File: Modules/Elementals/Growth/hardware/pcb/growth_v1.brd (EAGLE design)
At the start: 17.8 x 100 mm, 18 parts, among them J1 EURO_POWER, J2 WQP-PJ398SM6, J3 WQP-PJ398SM6, J4 WQP-PJ398SM6, J5 WQP-PJ398SM6, U1 TL072P

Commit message: Finalized(?)
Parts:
- R2, R3, R4, R6, R7, R8: device SonicAthame:0207/10 -> SonicAthame:0207/2V
- moved R7 21.6 mm to (1.91, 39.4), turned to 90 degrees
- moved R8 21.6 mm to (15.9, 39.4), turned to 270 degrees
- moved R3 14.0 mm to (1.91, 49.5)
- moved R4 7.01 mm to (8.89, 62.9), turned to 0 degrees
- moved R6 7.01 mm to (8.26, 24.1)
- moved C3 5.08 mm to (15.9, 44.5)
- moved C4 0.63 mm to (1.91, 45.1)
- moved R2 0.63 mm to (15.9, 49.5), turned to 270 degrees
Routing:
- net N$10: track 27.8 -> 6.77 mm
- net N$4: track 13.4 -> 31.5 mm
- net N$5: track 13.4 -> 3.65 mm
- net N$11: track 13.4 -> 3.65 mm
- net N$3: track 15.8 -> 6.77 mm
- net N$6: track 13.4 -> 21.8 mm
- net +12V: track 69.1 -> 73.7 mm
- net N$9: track 42.2 -> 39.0 mm
- net N$8: track 43.8 -> 46.1 mm
- net N$1: track 13.1 -> 10.9 mm
- net -12V: track 61.5 -> 62.8 mm
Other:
- board text added: "100x In"
- board text added: "100x Out"
- board text added: "100x Setting"
- board text added: "10x In"
- board text added: "10x Out"
- board text added: "10x Setting"
- board text added: "Elemental Growth"
- board text added: "Prototype v1"
- board text added: "Sonic Athame is fully open-hardware and open-software!! Find schematics and code on the official GitHub: https://github.com/nimaid/Sonic-Athame-eurorack"
- board text added: "Sonic Athame™"
- board text added: "The Point of Modular"

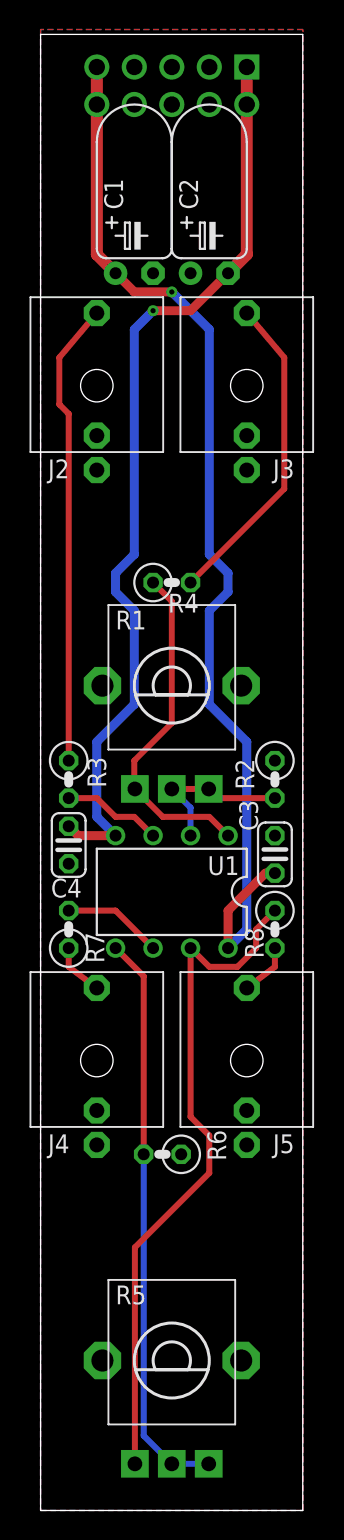
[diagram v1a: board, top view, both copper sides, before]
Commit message: Better power layout
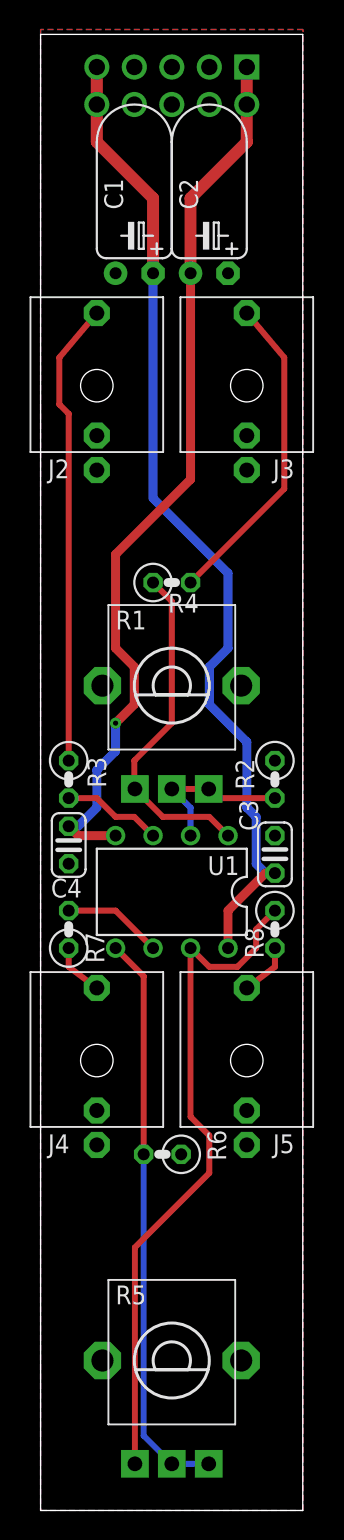
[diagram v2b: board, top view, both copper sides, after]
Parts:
- C1, C2: device SonicAthame:TT2D5L -> SonicAthame:TT2D5L_FLIP
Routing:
- net +12V: track 73.7 -> 67.8 mm, vias 1 -> 0
- net -12V: track 62.8 -> 61.3 mm
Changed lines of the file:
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@@
 </layers>
 <board>
-<fusionsync huburn="a.cGVyc29uYWw6dWUyZGY0M2Ex" projecturn="a.cGVyc29uYWw6dWUyZGY0M2ExIzIwMTkwODAzMjA2ODUyMzMx" f3durn="urn:adsk.wipprod:dm.lineage:vAaPX6FpQhacq-Y-F4SVOQ" pcbguid="a51a945c-d459-4631-a547-21d73037d6c1" lastpulledtime="" lastsyncedchangeguid="6d598e2e-e7a5-5e8d-0865-508f45d3280c"/>
+<fusionsync huburn="a.cGVyc29uYWw6dWUyZGY0M2Ex" projecturn="a.cGVyc29uYWw6dWUyZGY0M2ExIzIwMTkwODAzMjA2ODUyMzMx" f3durn="urn:adsk.wipprod:dm.lineage:vAaPX6FpQhacq-Y-F4SVOQ" pcbguid="a51a945c-d459-4631-a547-21d73037d6c1" lastpulledtime="" lastsyncedchangeguid="4652df98-1920-a6b8-155c-d7d488b7e636"/>
 <plain>
 <wire x1="0" y1="0" x2="17.76" y2="0" width="0" layer="20"/>
@@
 <attribute name="SPICEPREFIX" value="C" x="1.905" y="45.085" size="1.778" layer="27" rot="R270" display="off"/>
 </element>
-<element name="C1" library="SonicAthame" library_urn="urn:adsk.eagle:library:22327399" package="TT2D5L" package3d_urn="urn:adsk.eagle:package:26183890/3" value="10u" x="6.35" y="83.82" smashed="yes">
+<element name="C1" library="SonicAthame" library_urn="urn:adsk.eagle:library:22327399" package="TT2D5L_FLIP" package3d_urn="urn:adsk.eagle:package:26215121/2" value="10u" x="6.35" y="83.82" smashed="yes">
 <attribute name="NAME" x="4.318" y="88.138" size="1.27" layer="25" ratio="10" rot="R90" align="top-left"/>
 <attribute name="VALUE" x="8.128" y="88.138" size="1.27" layer="27" ratio="10" rot="R90"/>
 </element>
-<element name="C2" library="SonicAthame" library_urn="urn:adsk.eagle:library:22327399" package="TT2D5L" package3d_urn="urn:adsk.eagle:package:26183890/3" value="10u" x="11.43" y="83.82" smashed="yes">
+<element name="C2" library="SonicAthame" library_urn="urn:adsk.eagle:library:22327399" package="TT2D5L_FLIP" package3d_urn="urn:adsk.eagle:package:26215121/2" value="10u" x="11.43" y="83.82" smashed="yes">
 <attribute name="NAME" x="9.398" y="88.138" size="1.27" layer="25" ratio="10" rot="R90" align="top-left"/>
 <attribute name="VALUE" x="13.208" y="88.138" size="1.27" layer="27" ratio="10" rot="R90"/>
@@
 <contactref element="C1" pad="+"/>
 <wire x1="3.81" y1="97.79" x2="3.81" y2="95.25" width="0.8128" layer="1"/>
-<wire x1="3.81" y1="95.25" x2="3.81" y2="85.09" width="0.8128" layer="1"/>
-<wire x1="3.81" y1="85.09" x2="5.08" y2="83.82" width="0.8128" layer="1"/>
-<wire x1="5.08" y1="83.82" x2="6.35" y2="82.55" width="0.6096" layer="1"/>
-<wire x1="6.35" y1="82.55" x2="8.89" y2="82.55" width="0.6096" layer="1"/>
-<via x="8.89" y="82.55" extent="1-16" drill="0.35"/>
-<wire x1="11.43" y1="80.01" x2="8.89" y2="82.55" width="0.6096" layer="16"/>
-<wire x1="13.97" y1="39.37" x2="12.7" y2="38.1" width="0.6096" layer="16"/>
-<wire x1="13.97" y1="52.07" x2="11.43" y2="54.61" width="0.6096" layer="16"/>
-<wire x1="13.97" y1="52.07" x2="13.97" y2="39.37" width="0.6096" layer="16"/>
 <wire x1="12.7" y1="38.1" x2="12.7" y2="40.64" width="0.6096" layer="1"/>
 <wire x1="15.875" y1="43.18" x2="15.24" y2="43.18" width="0.6096" layer="1"/>
 <wire x1="15.24" y1="43.18" x2="12.7" y2="40.64" width="0.6096" layer="1"/>
-<wire x1="11.43" y1="54.61" x2="11.43" y2="60.96" width="0.6096" layer="16"/>
-<wire x1="11.43" y1="60.96" x2="12.7" y2="62.23" width="0.6096" layer="16"/>
-<wire x1="12.7" y1="62.23" x2="12.7" y2="63.5" width="0.6096" layer="16"/>
-<wire x1="12.7" y1="63.5" x2="11.43" y2="64.77" width="0.6096" layer="16"/>
-<wire x1="11.43" y1="64.77" x2="11.43" y2="80.01" width="0.6096" layer="16"/>
+<wire x1="7.62" y1="88.9" x2="7.62" y2="83.82" width="0.8128" layer="1"/>
+<wire x1="3.81" y1="95.25" x2="3.81" y2="92.71" width="0.8128" layer="1"/>
+<wire x1="3.81" y1="92.71" x2="7.62" y2="88.9" width="0.8128" layer="1"/>
+<wire x1="7.62" y1="68.58" x2="12.7" y2="63.5" width="0.6096" layer="16"/>
+<wire x1="12.7" y1="58.42" x2="11.43" y2="57.15" width="0.6096" layer="16"/>
+<wire x1="13.97" y1="47.625" x2="14.605" y2="46.99" width="0.6096" layer="16"/>
+<wire x1="14.605" y1="46.99" x2="14.605" y2="43.815" width="0.6096" layer="16"/>
+<wire x1="14.605" y1="43.815" x2="15.24" y2="43.18" width="0.6096" layer="16"/>
+<wire x1="15.24" y1="43.18" x2="15.875" y2="43.18" width="0.6096" layer="16"/>
+<wire x1="7.62" y1="83.82" x2="7.62" y2="68.58" width="0.6096" layer="16"/>
+<wire x1="12.7" y1="63.5" x2="12.7" y2="58.42" width="0.6096" layer="16"/>
+<wire x1="11.43" y1="57.15" x2="11.43" y2="54.61" width="0.6096" layer="16"/>
+<wire x1="11.43" y1="54.61" x2="13.97" y2="52.07" width="0.6096" layer="16"/>
+<wire x1="13.97" y1="52.07" x2="13.97" y2="47.625" width="0.6096" layer="16"/>
 </signal>
 <signal name="-12V">
@@
 <contactref element="C2" pad="-"/>
 <wire x1="13.97" y1="97.79" x2="13.97" y2="95.25" width="0.8128" layer="1"/>
-<wire x1="13.97" y1="95.25" x2="13.97" y2="85.09" width="0.8128" layer="1"/>
-<wire x1="13.97" y1="85.09" x2="12.7" y2="83.82" width="0.8128" layer="1"/>
-<wire x1="12.7" y1="83.82" x2="10.16" y2="81.28" width="0.6096" layer="1"/>
-<wire x1="10.16" y1="81.28" x2="7.62" y2="81.28" width="0.6096" layer="1"/>
-<via x="7.62" y="81.28" extent="1-16" drill="0.35"/>
-<wire x1="6.35" y1="80.01" x2="7.62" y2="81.28" width="0.6096" layer="16"/>
-<wire x1="3.81" y1="46.99" x2="5.08" y2="45.72" width="0.6096" layer="16"/>
-<wire x1="3.81" y1="52.07" x2="6.35" y2="54.61" width="0.6096" layer="16"/>
-<wire x1="3.81" y1="52.07" x2="3.81" y2="46.99" width="0.6096" layer="16"/>
 <wire x1="5.08" y1="45.72" x2="2.54" y2="45.72" width="0.6096" layer="1"/>
 <wire x1="2.54" y1="45.72" x2="1.905" y2="46.355" width="0.6096" layer="1"/>
-<wire x1="6.35" y1="54.61" x2="6.35" y2="60.96" width="0.6096" layer="16"/>
-<wire x1="6.35" y1="60.96" x2="5.08" y2="62.23" width="0.6096" layer="16"/>
-<wire x1="5.08" y1="62.23" x2="5.08" y2="63.5" width="0.6096" layer="16"/>
-<wire x1="5.08" y1="63.5" x2="6.35" y2="64.77" width="0.6096" layer="16"/>
-<wire x1="6.35" y1="64.77" x2="6.35" y2="80.01" width="0.6096" layer="16"/>
+<wire x1="13.97" y1="95.25" x2="13.97" y2="92.71" width="0.8128" layer="1"/>
+<wire x1="13.97" y1="92.71" x2="10.16" y2="88.9" width="0.8128" layer="1"/>
+<wire x1="10.16" y1="88.9" x2="10.16" y2="83.82" width="0.8128" layer="1"/>
+<wire x1="10.16" y1="83.82" x2="10.16" y2="69.85" width="0.6096" layer="1"/>
+<wire x1="10.16" y1="69.85" x2="5.08" y2="64.77" width="0.6096" layer="1"/>
+<wire x1="5.08" y1="58.42" x2="6.35" y2="57.15" width="0.6096" layer="1"/>
+<wire x1="6.35" y1="57.15" x2="6.35" y2="54.61" width="0.6096" layer="1"/>
+<wire x1="6.35" y1="54.61" x2="5.08" y2="53.34" width="0.6096" layer="1"/>
+<via x="5.08" y="53.34" extent="1-16" drill="0.35"/>
+<wire x1="5.08" y1="53.34" x2="5.08" y2="51.435" width="0.6096" layer="16"/>
+<wire x1="5.08" y1="51.435" x2="3.81" y2="50.165" width="0.6096" layer="16"/>
+<wire x1="3.81" y1="50.165" x2="3.81" y2="47.625" width="0.6096" layer="16"/>
+<wire x1="3.81" y1="47.625" x2="2.54" y2="46.355" width="0.6096" layer="16"/>
+<wire x1="2.54" y1="46.355" x2="1.905" y2="46.355" width="0.6096" layer="16"/>
+<wire x1="5.08" y1="64.77" x2="5.08" y2="58.42" width="0.6096" layer="1"/>
 </signal>
 <signal name="GND">
